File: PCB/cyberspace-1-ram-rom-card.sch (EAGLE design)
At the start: 15 parts, among them U1 IO PLD, U3 BANK PLD, U4 SRAM 32Kx8, U5 ROM 256K, U6 SRAM 32Kx8

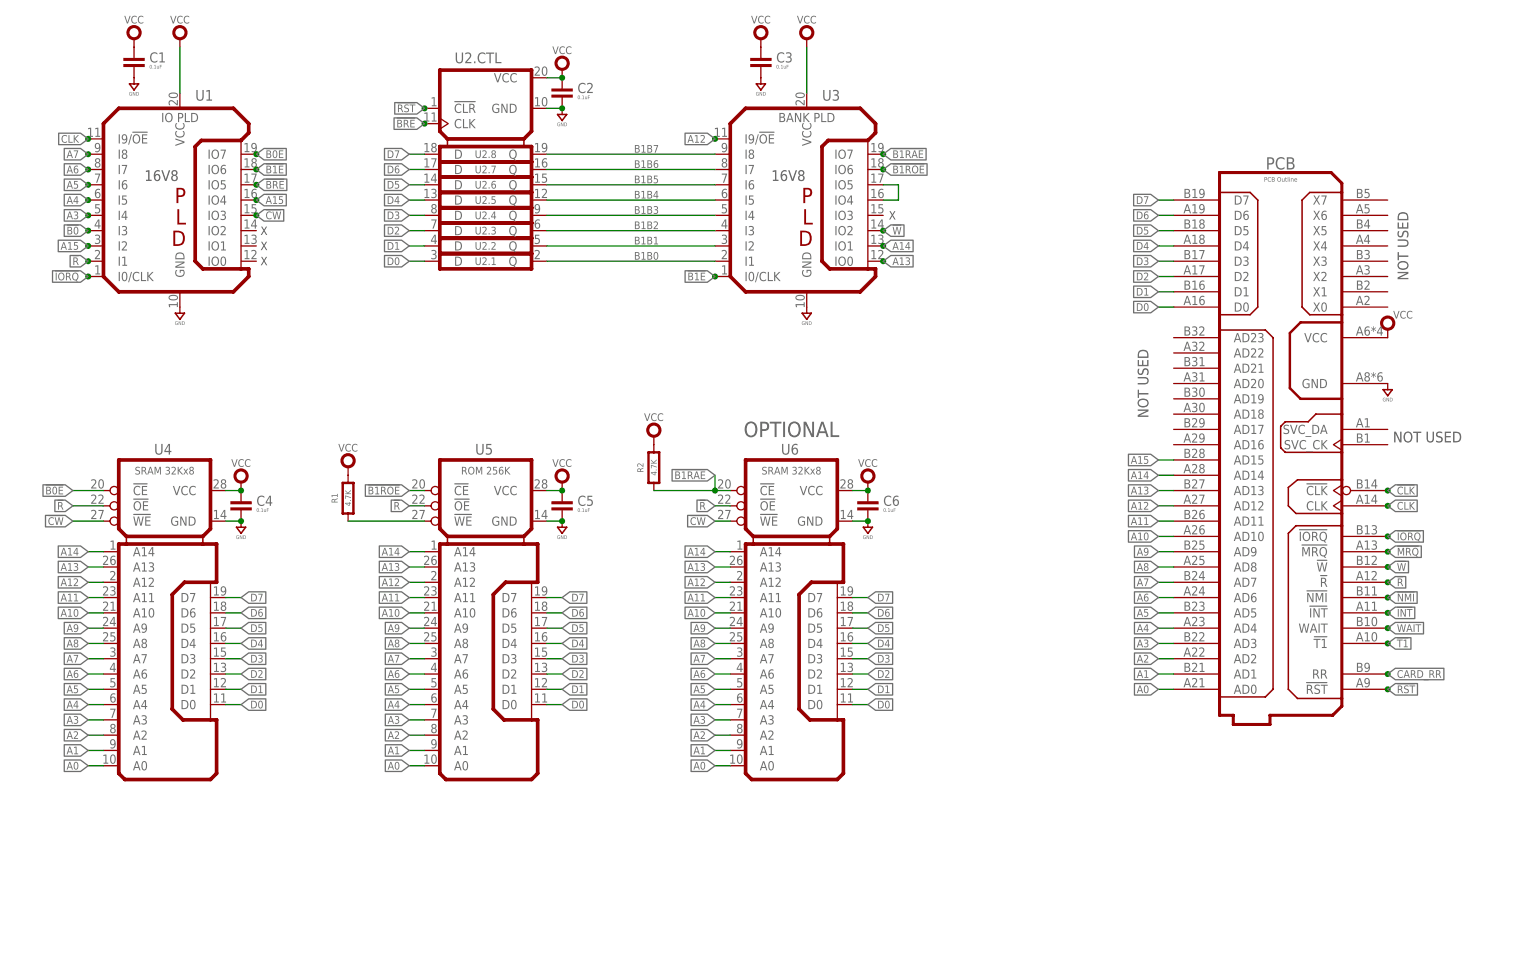
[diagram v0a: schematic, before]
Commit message: Routed RAM-ROM card. Almost there.
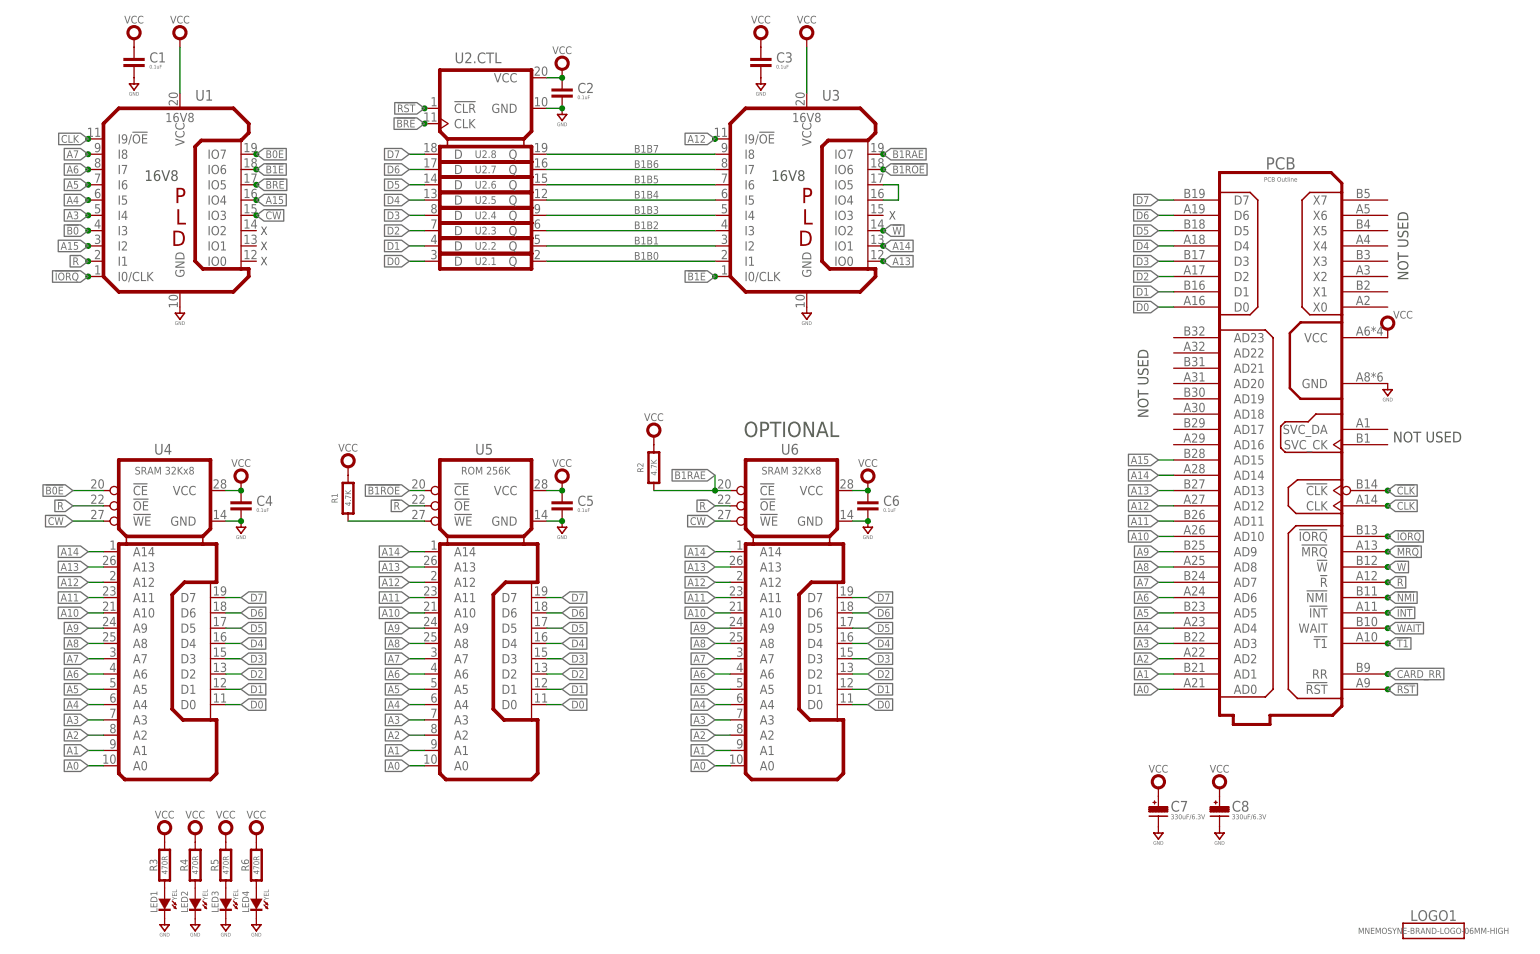
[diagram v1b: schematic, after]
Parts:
- added C7, C8: 330uF/6.3V, rlc:CAPACITOR_POL-ALUM-SMT-6.3
- added LED1, LED2, LED3, LED4: YEL, led:SMT0603
- added LOGO1: MNEMOSYNE-BRAND-LOGO-06MM-HIGH, gfx-glyphs:MNEMOSYNE-BRAND-LOGO-06MM-HIGH
- added R3, R4, R5, R6: 470R, rlc:RESISTOR0603
- U1: value IO PLD -> 16V8
- U3: value BANK PLD -> 16V8
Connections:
- new net N$2: LED1.A, R3.1
- new net N$3: LED2.A, R4.1
- new net N$5: LED3.A, R5.1
- new net N$6: LED4.A, R6.1
- net GND: now also C7.N, C8.N, LED1.C, LED2.C, LED3.C, LED4.C
- net VCC: now also C7.P, C8.P, R3.2, R4.2, R5.2, R6.2

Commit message: New RamRom using flash chip.
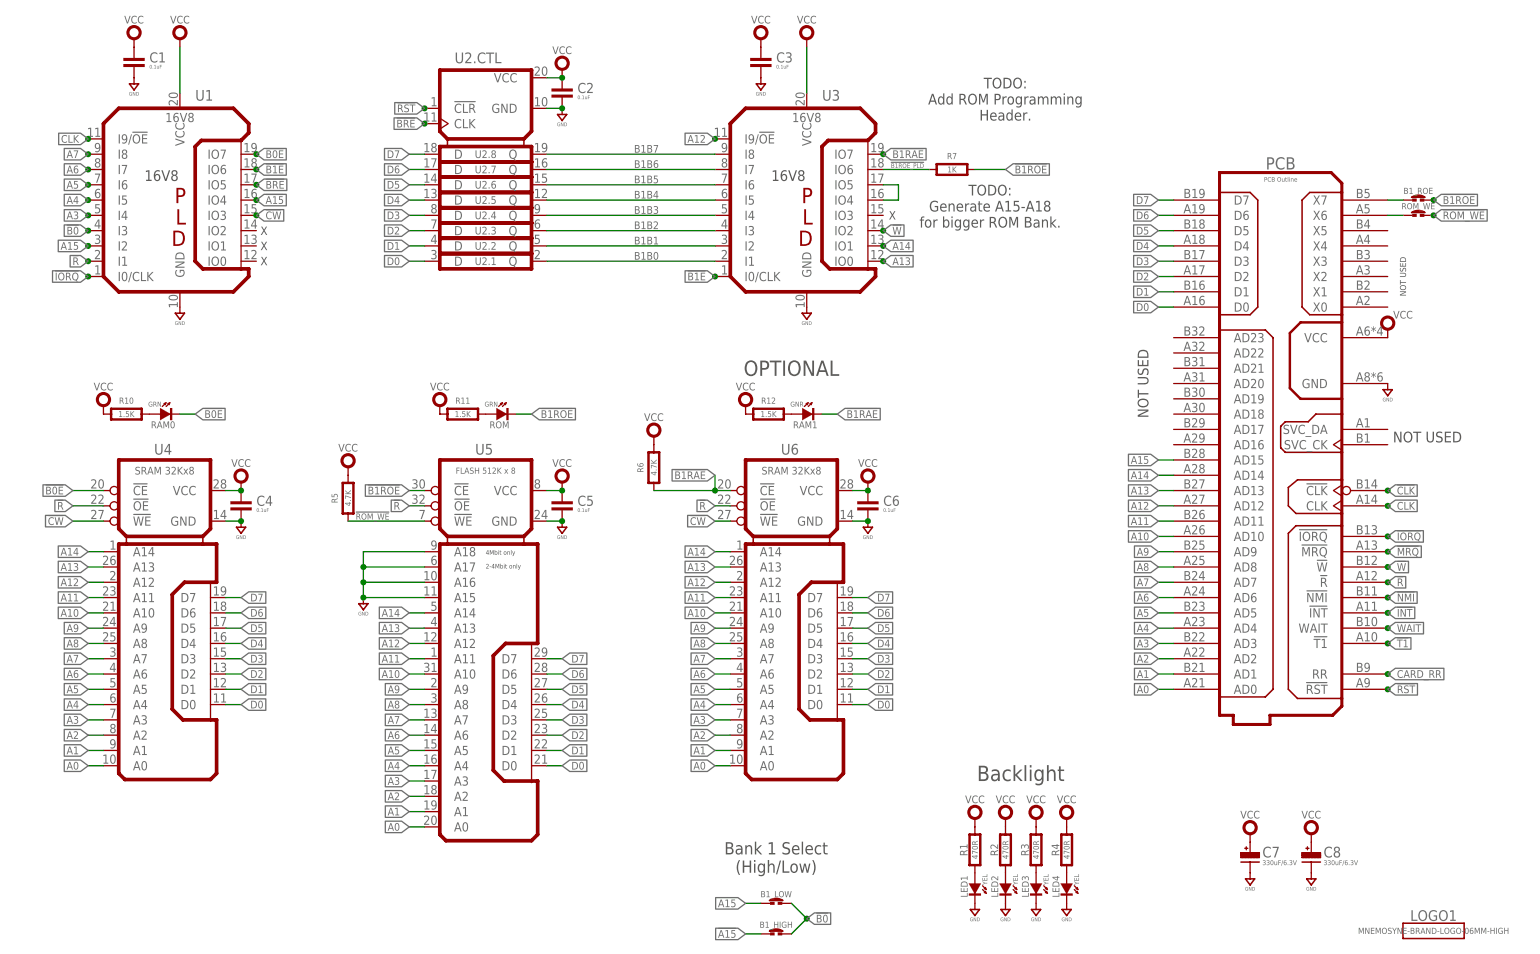
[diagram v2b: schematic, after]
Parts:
- added B1_HIGH, B1_LOW, B1_ROE, ROM_WE: (no value), rlc:SOLDER_JUMPER-60MIL-RND
- added R10, R11, R12: 1.5K, rlc:RESISTOR0603
- added R7: 1K, rlc:RESISTOR0603
- added RAM0, ROM: GRN, led:SMT0603
- added RAM1: GNR, led:SMT0603
- R1, R2: value 4.7K -> 470R
- R5, R6: value 470R -> 4.7K
- U5: value ROM 256K -> FLASH 512K x 8; device logic:28C256SU -> logic:FLASH_512KX8-512K-TSOP
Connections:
- new net !B1ROE_PLD: R7.1, U3.IO6
- new net !ROM_WE: R5.1, ROM_WE.P$2, U5.!WE
- new net N$10: PCB.X6, ROM_WE.P$1
- new net N$7: R11.2, ROM.A
- new net N$8: R12.2, RAM1.A
- new net N$9: B1_ROE.P$1, PCB.X7
- net !A15: now also B1_HIGH.P$1
- net !B0: now also B1_HIGH.P$2, B1_LOW.P$2
- net !B0E: now also RAM0.C
- net !B1RAE: now also R6.1, RAM1.C; no longer R2.1
- net !B1ROE: now also B1_ROE.P$2, R7.2, ROM.C; no longer U3.IO6
- net A15: now also B1_LOW.P$1
- net GND: now also U5.A15, U5.A16, U5.A17, U5.A18
- net N$2: now also R1.1; no longer R3.1
- net N$3: now also R2.1; no longer R4.1
- net N$4: now also R10.2, RAM0.A; no longer R1.1, U5.!WE
- net N$5: now also R3.1; no longer R5.1
- net N$6: now also R4.1; no longer R6.1
- net VCC: now also R10.1, R11.1, R12.1
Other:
- note added: "Backlight"
- note added: "Bank 1 Select (High/Low)"
- note added: "TODO: Add ROM Programming Header."
- note added: "TODO: Generate A15-A18 for bigger ROM Bank."
- moved on the sheet: C7, C8, LED1, LED2, LED3, LED4, R1, R2, R3, R4, R5, R6

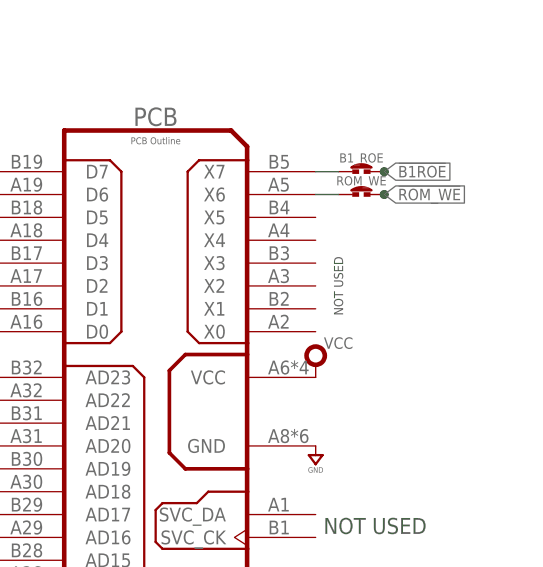
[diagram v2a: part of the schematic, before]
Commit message: Add notes on edge connector.
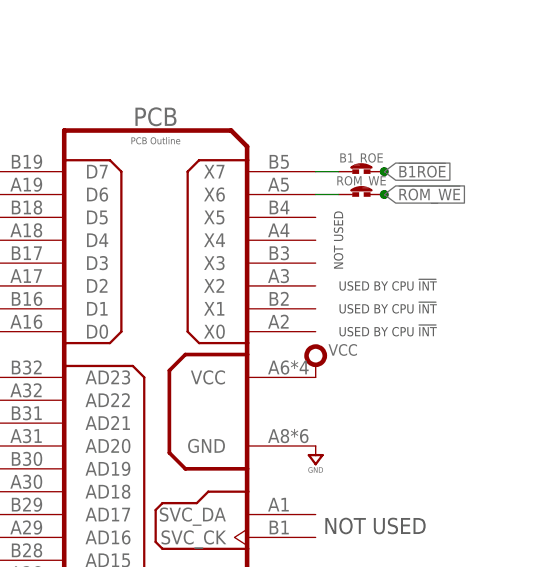
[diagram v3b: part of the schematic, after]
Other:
- note added: "USED BY CPU !INT"
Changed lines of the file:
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@@
 <plain>
 <text x="208.28" y="104.14" size="1.778" layer="97" rot="R90" align="center">NOT USED</text>
-<text x="251.46" y="121.92" size="1.016" layer="97" rot="R90" align="center">NOT USED</text>
+<text x="251.46" y="127" size="1.016" layer="97" rot="R90" align="center">NOT USED</text>
 <text x="255.524" y="95.25" size="1.778" layer="97" rot="R180" align="center">NOT USED</text>
 <text x="62.23" y="127" size="1.397" layer="97" distance="80" align="center">X
@@
 <text x="147.32" y="22.86" size="2.032" layer="97" ratio="12" align="bottom-center">Bank 1 Select
 (High/Low)</text>
+<text x="251.46" y="121.92" size="1.016" layer="97" align="center-left">USED BY CPU !INT</text>
+<text x="251.46" y="119.38" size="1.016" layer="97" align="center-left">USED BY CPU !INT</text>
+<text x="251.46" y="116.84" size="1.016" layer="97" align="center-left">USED BY CPU !INT</text>
 </plain>
 <instances>
@@
 </instance>
 <instance part="SUPPLY13" gate="G$1" x="248.92" y="111.76" smashed="yes">
-<attribute name="VALUE" x="251.46" y="114.935" size="1.27" layer="96" font="vector" ratio="15" align="bottom-center"/>
+<attribute name="VALUE" x="251.968" y="114.173" size="1.27" layer="96" font="vector" ratio="15" align="bottom-center"/>
 </instance>
 <instance part="SUPPLY16" gate="G$1" x="48.26" y="160.02" smashed="yes">
